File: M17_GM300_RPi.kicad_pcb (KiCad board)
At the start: 4 copper layers, 85 x 56 mm, 54 parts, among them J1 RJ45, J2 SJ1-3523N, J3 1935161, J4 DB9_Female, J5 RPi Header, Q1 BSS138, Q2 BSS138, Q3 BSS138, Q4 BSS138, SW1 SW_Push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

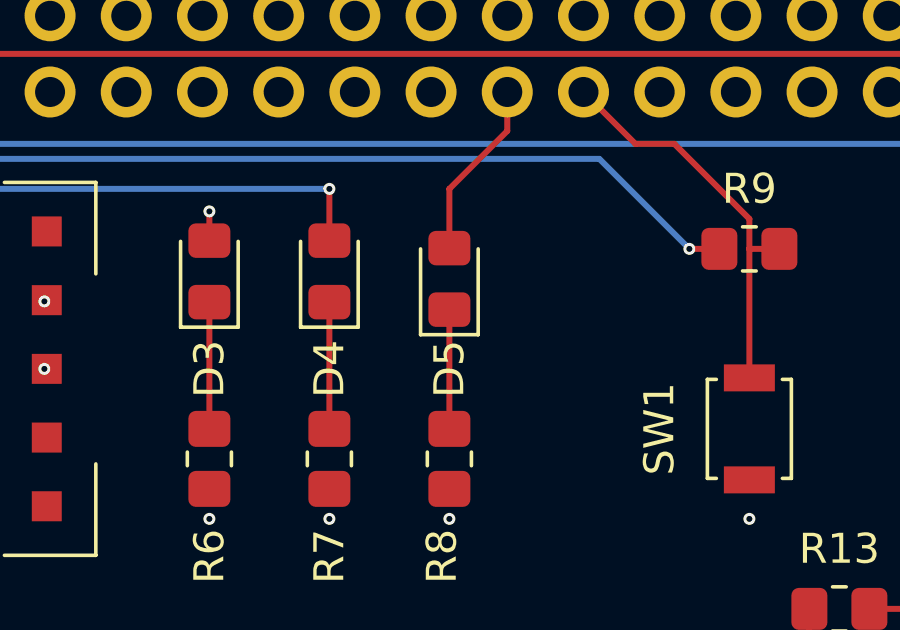
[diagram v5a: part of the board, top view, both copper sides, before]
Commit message: push D5 up a bit, add models
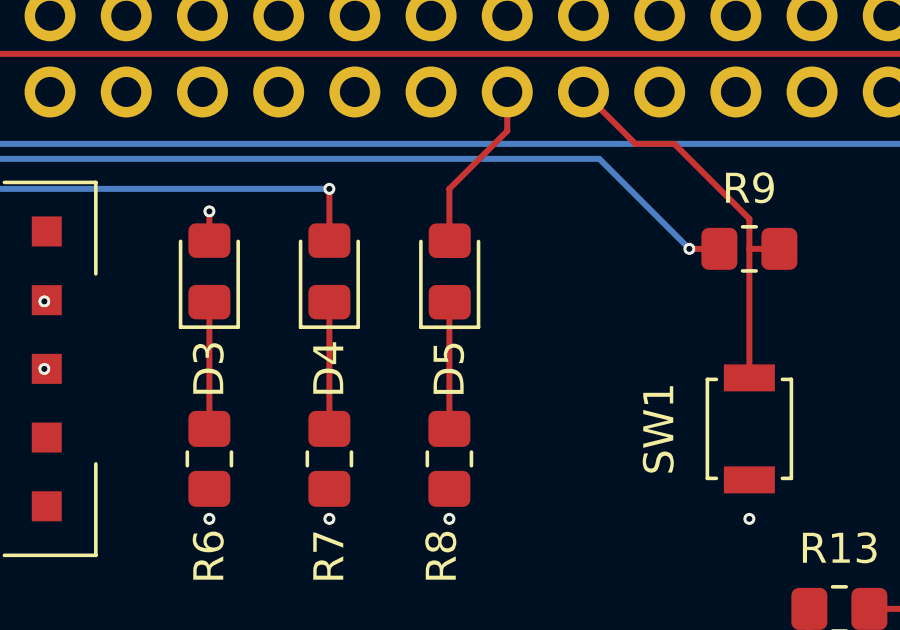
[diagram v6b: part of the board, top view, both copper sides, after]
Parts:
- moved D5 0.25 mm to (207.0, 60.8)

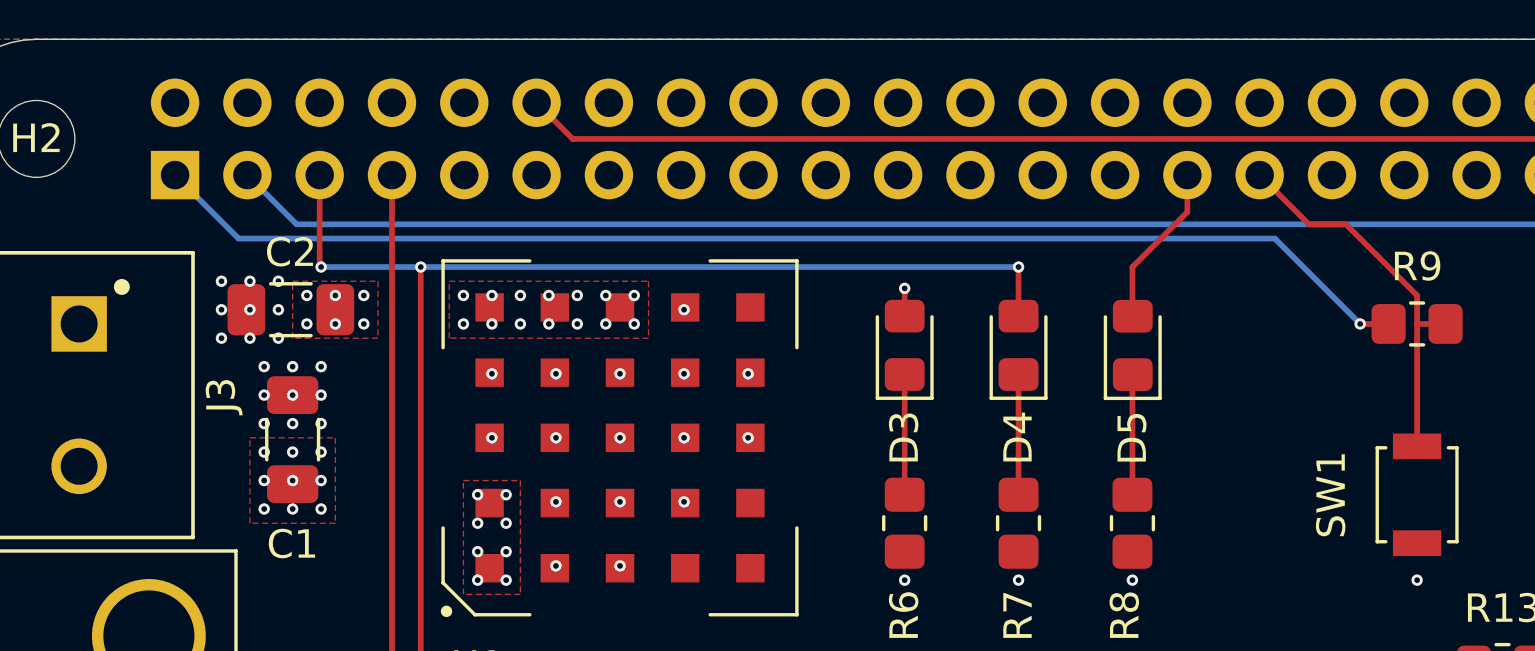
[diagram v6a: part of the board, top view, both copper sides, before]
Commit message: updated 3v3 power trace, led alignments
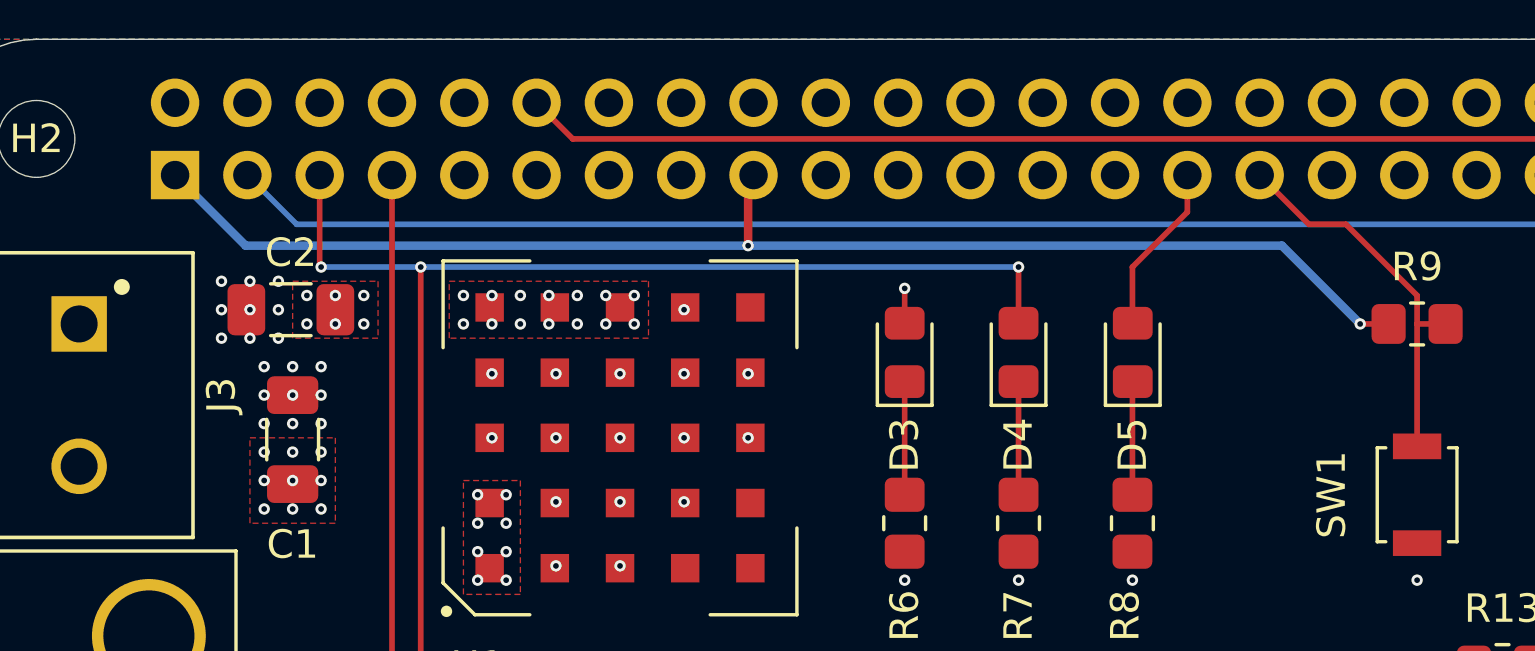
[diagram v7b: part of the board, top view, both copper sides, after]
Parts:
- moved D3 0.25 mm to (199.0, 61.0)
- moved D4 0.25 mm to (203.0, 61.0)
- moved D5 0.25 mm to (207.0, 61.0)
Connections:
- J5 pad 17: Net-(J5-Pad17) -> +3V3
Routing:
- net +3V3: track 53.2 -> 55.8 mm, vias 7 -> 8

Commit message: change c1 c2, update bom
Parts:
- C1, C2: value 1000 uF -> 47 uF
